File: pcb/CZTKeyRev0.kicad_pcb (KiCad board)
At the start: 2 copper layers, 327.8 x 176.2 mm, 166 parts, among them U1 proton_c

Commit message: Edits to layout and sutff
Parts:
- removed D73: D_Small, Diode_THT:D_DO-35_SOD27_P5.08mm_Vertical_KathodeUp
- moved D45 487.8 mm to (57.8, 36.5), turned to 270 degrees
- moved D30 485.9 mm to (54.6, 36.5), turned to 270 degrees
- moved D15 436.1 mm to (51.4, 36.5), turned to 270 degrees
- moved D1 27.2 mm to (48.3, 36.5)
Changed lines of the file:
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@@
     (tracks 0)
     (zones 0)
-    (modules 166)
+    (modules 165)
     (nets 154)
   )
@@
   )
   (module Diode_THT:D_DO-35_SOD27_P5.08mm_Vertical_KathodeUp (layer F.Cu)
-    (at 182.41375 -185.63375)
-    (descr "Diode, DO-35_SOD27 series, Axial, Vertical, pin pitch=5.08mm, , length*diameter=4*2mm^2, , http://www.diodes.com/_files/packages/DO-35.pdf")
-    (tags "Diode DO-35_SOD27 series Axial Vertical pin pitch 5.08mm  length 4mm diameter 2mm")
-    (fp_text reference D73 (at 2.54 -2.326371) (layer F.SilkS)
-      (effects (font (size 1 1) (thickness 0.15)))
-    )
-    (fp_text value D_Small (at 2.54 2.326371) (layer F.Fab)
-      (effects (font (size 1 1) (thickness 0.15)))
-    )
-    (fp_text user K (at 1.5 0.8) (layer F.SilkS)
-      (effects (font (size 1 1) (thickness 0.15)))
-    )
-    (fp_text user K (at 1.5 0.8) (layer F.Fab)
-      (effects (font (size 1 1) (thickness 0.15)))
-    )
-    (fp_text user %R (at 2.54 -2.326371) (layer F.Fab)
-      (effects (font (size 1 1) (thickness 0.15)))
-    )
-    (fp_line (start 6.33 -1.25) (end -1.05 -1.25) (layer F.CrtYd) (width 0.05))
-    (fp_line (start 6.33 1.25) (end 6.33 -1.25) (layer F.CrtYd) (width 0.05))
-    (fp_line (start -1.05 1.25) (end 6.33 1.25) (layer F.CrtYd) (width 0.05))
-    (fp_line (start -1.05 -1.25) (end -1.05 1.25) (layer F.CrtYd) (width 0.05))
-    (fp_line (start 3.753629 0) (end 1.1 0) (layer F.SilkS) (width 0.12))
-    (fp_line (start 0 0) (end 5.08 0) (layer F.Fab) (width 0.1))
-    (fp_circle (center 5.08 0) (end 6.406371 0) (layer F.SilkS) (width 0.12))
-    (fp_circle (center 5.08 0) (end 6.08 0) (layer F.Fab) (width 0.1))
-    (pad 2 thru_hole oval (at 5.08 0) (size 1.6 1.6) (drill 0.8) (layers *.Cu *.Mask)
-      (net 78 "Net-(D73-Pad2)"))
-    (pad 1 thru_hole rect (at 0 0) (size 1.6 1.6) (drill 0.8) (layers *.Cu *.Mask)
-      (net 79 ROW5))
-    (model ${KISYS3DMOD}/Diode_THT.3dshapes/D_DO-35_SOD27_P5.08mm_Vertical_KathodeUp.wrl
-      (at (xyz 0 0 0))
-      (scale (xyz 1 1 1))
-      (rotate (xyz 0 0 0))
-    )
-  )
-  (module Diode_THT:D_DO-35_SOD27_P5.08mm_Vertical_KathodeUp (layer F.Cu)
     (at 189.10375 -99.81375)
     (descr "Diode, DO-35_SOD27 series, Axial, Vertical, pin pitch=5.08mm, , length*diameter=4*2mm^2, , http://www.diodes.com/_files/packages/DO-35.pdf")
@@
   )
   (module Diode_THT:D_DO-35_SOD27_P5.08mm_Vertical_KathodeUp (layer F.Cu)
-    (at 448.90375 -255.05375)
+    (at 57.785 36.5125 270)
     (descr "Diode, DO-35_SOD27 series, Axial, Vertical, pin pitch=5.08mm, , length*diameter=4*2mm^2, , http://www.diodes.com/_files/packages/DO-35.pdf")
     (tags "Diode DO-35_SOD27 series Axial Vertical pin pitch 5.08mm  length 4mm diameter 2mm")
-    (fp_text reference D45 (at 2.54 -2.326371) (layer F.SilkS)
+    (fp_text reference D45 (at 2.54 -2.326371 90) (layer F.SilkS)
       (effects (font (size 1 1) (thickness 0.15)))
     )
-    (fp_text value D_Small (at 2.54 2.326371) (layer F.Fab)
+    (fp_text value D_Small (at 2.54 2.326371 90) (layer F.Fab)
       (effects (font (size 1 1) (thickness 0.15)))
     )
-    (fp_text user K (at 1.5 0.8) (layer F.SilkS)
+    (fp_text user K (at 1.5 0.8 90) (layer F.SilkS)
       (effects (font (size 1 1) (thickness 0.15)))
     )
-    (fp_text user K (at 1.5 0.8) (layer F.Fab)
+    (fp_text user K (at 1.5 0.8 90) (layer F.Fab)
       (effects (font (size 1 1) (thickness 0.15)))
     )
-    (fp_text user %R (at 2.54 -2.326371) (layer F.Fab)
+    (fp_text user %R (at 2.54 -2.326371 90) (layer F.Fab)
       (effects (font (size 1 1) (thickness 0.15)))
     )
@@
     (fp_circle (center 5.08 0) (end 6.406371 0) (layer F.SilkS) (width 0.12))
     (fp_circle (center 5.08 0) (end 6.08 0) (layer F.Fab) (width 0.1))
-    (pad 2 thru_hole oval (at 5.08 0) (size 1.6 1.6) (drill 0.8) (layers *.Cu *.Mask)
+    (pad 2 thru_hole oval (at 5.08 0 270) (size 1.6 1.6) (drill 0.8) (layers *.Cu *.Mask)
       (net 48 "Net-(D45-Pad2)"))
-    (pad 1 thru_hole rect (at 0 0) (size 1.6 1.6) (drill 0.8) (layers *.Cu *.Mask)
+    (pad 1 thru_hole rect (at 0 0 270) (size 1.6 1.6) (drill 0.8) (layers *.Cu *.Mask)
       (net 49 ROW3))
     (model ${KISYS3DMOD}/Diode_THT.3dshapes/D_DO-35_SOD27_P5.08mm_Vertical_KathodeUp.wrl
@@
   )
   (module Diode_THT:D_DO-35_SOD27_P5.08mm_Vertical_KathodeUp (layer F.Cu)
-    (at 448.90375 -247.51375)
+    (at 54.61 36.5125 270)
     (descr "Diode, DO-35_SOD27 series, Axial, Vertical, pin pitch=5.08mm, , length*diameter=4*2mm^2, , http://www.diodes.com/_files/packages/DO-35.pdf")
     (tags "Diode DO-35_SOD27 series Axial Vertical pin pitch 5.08mm  length 4mm diameter 2mm")
-    (fp_text reference D30 (at 2.54 -2.326371) (layer F.SilkS)
+    (fp_text reference D30 (at 2.54 -2.326371 90) (layer F.SilkS)
       (effects (font (size 1 1) (thickness 0.15)))
     )
-    (fp_text value D_Small (at 2.54 2.326371) (layer F.Fab)
+    (fp_text value D_Small (at 2.54 2.326371 90) (layer F.Fab)
       (effects (font (size 1 1) (thickness 0.15)))
     )
-    (fp_text user K (at 1.5 0.8) (layer F.SilkS)
+    (fp_text user K (at 1.5 0.8 90) (layer F.SilkS)
       (effects (font (size 1 1) (thickness 0.15)))
     )
-    (fp_text user K (at 1.5 0.8) (layer F.Fab)
+    (fp_text user K (at 1.5 0.8 90) (layer F.Fab)
       (effects (font (size 1 1) (thickness 0.15)))
     )
-    (fp_text user %R (at 2.54 -2.326371) (layer F.Fab)
+    (fp_text user %R (at 2.54 -2.326371 90) (layer F.Fab)
       (effects (font (size 1 1) (thickness 0.15)))
     )
@@
     (fp_circle (center 5.08 0) (end 6.406371 0) (layer F.SilkS) (width 0.12))
     (fp_circle (center 5.08 0) (end 6.08 0) (layer F.Fab) (width 0.1))
-    (pad 2 thru_hole oval (at 5.08 0) (size 1.6 1.6) (drill 0.8) (layers *.Cu *.Mask)
+    (pad 2 thru_hole oval (at 5.08 0 270) (size 1.6 1.6) (drill 0.8) (layers *.Cu *.Mask)
       (net 32 "Net-(D30-Pad2)"))
-    (pad 1 thru_hole rect (at 0 0) (size 1.6 1.6) (drill 0.8) (layers *.Cu *.Mask)
+    (pad 1 thru_hole rect (at 0 0 270) (size 1.6 1.6) (drill 0.8) (layers *.Cu *.Mask)
       (net 33 ROW2))
     (model ${KISYS3DMOD}/Diode_THT.3dshapes/D_DO-35_SOD27_P5.08mm_Vertical_KathodeUp.wrl
@@
   )
   (module Diode_THT:D_DO-35_SOD27_P5.08mm_Vertical_KathodeUp (layer F.Cu)
-    (at 423.65375 -190.68375)
+    (at 51.435 36.5125 270)
     (descr "Diode, DO-35_SOD27 series, Axial, Vertical, pin pitch=5.08mm, , length*diameter=4*2mm^2, , http://www.diodes.com/_files/packages/DO-35.pdf")
     (tags "Diode DO-35_SOD27 series Axial Vertical pin pitch 5.08mm  length 4mm diameter 2mm")
-    (fp_text reference D15 (at 2.54 -2.326371) (layer F.SilkS)
+    (fp_text reference D15 (at 2.54 -2.326371 90) (layer F.SilkS)
       (effects (font (size 1 1) (thickness 0.15)))
     )
-    (fp_text value D_Small (at 2.54 2.326371) (layer F.Fab)
+    (fp_text value D_Small (at 2.54 2.326371 90) (layer F.Fab)
       (effects (font (size 1 1) (thickness 0.15)))
     )
-    (fp_text user K (at 1.5 0.8) (layer F.SilkS)
+    (fp_text user K (at 1.5 0.8 90) (layer F.SilkS)
       (effects (font (size 1 1) (thickness 0.15)))
     )
-    (fp_text user K (at 1.5 0.8) (layer F.Fab)
+    (fp_text user K (at 1.5 0.8 90) (layer F.Fab)
       (effects (font (size 1 1) (thickness 0.15)))
     )
-    (fp_text user %R (at 2.54 -2.326371) (layer F.Fab)
+    (fp_text user %R (at 2.54 -2.326371 90) (layer F.Fab)
       (effects (font (size 1 1) (thickness 0.15)))
     )
@@
     (fp_circle (center 5.08 0) (end 6.406371 0) (layer F.SilkS) (width 0.12))
     (fp_circle (center 5.08 0) (end 6.08 0) (layer F.Fab) (width 0.1))
-    (pad 2 thru_hole oval (at 5.08 0) (size 1.6 1.6) (drill 0.8) (layers *.Cu *.Mask)
+    (pad 2 thru_hole oval (at 5.08 0 270) (size 1.6 1.6) (drill 0.8) (layers *.Cu *.Mask)
       (net 16 "Net-(D15-Pad2)"))
-    (pad 1 thru_hole rect (at 0 0) (size 1.6 1.6) (drill 0.8) (layers *.Cu *.Mask)
+    (pad 1 thru_hole rect (at 0 0 270) (size 1.6 1.6) (drill 0.8) (layers *.Cu *.Mask)
       (net 17 ROW1))
     (model ${KISYS3DMOD}/Diode_THT.3dshapes/D_DO-35_SOD27_P5.08mm_Vertical_KathodeUp.wrl
@@
   )
   (module Diode_THT:D_DO-35_SOD27_P5.08mm_Vertical_KathodeUp (layer F.Cu)
-    (at 75.40625 34.925 270)
+    (at 48.26 36.5125 270)
     (descr "Diode, DO-35_SOD27 series, Axial, Vertical, pin pitch=5.08mm, , length*diameter=4*2mm^2, , http://www.diodes.com/_files/packages/DO-35.pdf")
     (tags "Diode DO-35_SOD27 series Axial Vertical pin pitch 5.08mm  length 4mm diameter 2mm")

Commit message: Positioned things
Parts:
- added C1: 100n, Capacitor_SMD:C_0603_1608Metric, F.Cu at (12.7, 77.0)
- added C2: 100n, Capacitor_SMD:C_0603_1608Metric, F.Cu at (-10.3, 77.0)
- added D73: D_Small, Diode_THT:D_DO-35_SOD27_P5.08mm_Vertical_KathodeUp, F.Cu at (197.6, 46.0)
- added D82: D_Small, Diode_THT:D_DO-35_SOD27_P5.08mm_Vertical_KathodeUp, F.Cu at (53.2, 46.0)
- added D83: D_Small, Diode_THT:D_DO-35_SOD27_P5.08mm_Vertical_KathodeUp, F.Cu at (56.4, 46.0)
- added D84: D_Small, Diode_THT:D_DO-35_SOD27_P5.08mm_Vertical_KathodeUp, F.Cu at (59.5, 46.0)
- added D85: D_Small, Diode_THT:D_DO-35_SOD27_P5.08mm_Vertical_KathodeUp, F.Cu at (62.7, 46.0)
- added D86: D_Small, Diode_THT:D_DO-35_SOD27_P5.08mm_Vertical_KathodeUp, F.Cu at (65.9, 46.0)
- added MX_MAC1: MX-NoLED, MX_Alps_Hybrid:MX-1U-NoLED, F.Cu at (1.59, 104.8)
- added MX_MAC2: MX-NoLED, MX_Alps_Hybrid:MX-1U-NoLED, F.Cu at (1.59, 123.8)
- added MX_MAC3: MX-NoLED, MX_Alps_Hybrid:MX-1U-NoLED, F.Cu at (1.59, 142.9)
- added MX_MAC4: MX-NoLED, MX_Alps_Hybrid:MX-1U-NoLED, F.Cu at (1.59, 161.9)
- added MX_MAC5: MX-NoLED, MX_Alps_Hybrid:MX-1U-NoLED, F.Cu at (1.59, 181.0)
- added R1: 10k, Resistor_SMD:R_Array_Convex_4x0603, F.Cu at (-9.53, 87.3)
- added R2: 10k, Resistor_SMD:R_Array_Convex_4x0603, F.Cu at (11.9, 87.3)
- added R3: 10K, Resistor_SMD:R_Array_Convex_4x0603, F.Cu at (-9.53, 82.5)
- added R4: 10K, Resistor_SMD:R_Array_Convex_4x0603, F.Cu at (11.9, 82.5)
- added R5: 10K, Resistor_SMD:R_0603_1608Metric, F.Cu at (303.7, 62.0)
- added WS1: WS2812B, WS2812B-edited:Neopixel_easy_LED_WS2812B_PLCC4_5.0x5.0mm_P3.2mm, F.Cu at (25.2, 74.0)
- added WS10: WS2812B, WS2812B-edited:Neopixel_easy_LED_WS2812B_PLCC4_5.0x5.0mm_P3.2mm, F.Cu at (211.2, 74.0)
- added WS11: WS2812B, WS2812B-edited:Neopixel_easy_LED_WS2812B_PLCC4_5.0x5.0mm_P3.2mm, F.Cu at (230.2, 74.0)
- added WS12: WS2812B, WS2812B-edited:Neopixel_easy_LED_WS2812B_PLCC4_5.0x5.0mm_P3.2mm, F.Cu at (249.2, 74.0)
- added WS13: WS2812B, WS2812B-edited:Neopixel_easy_LED_WS2812B_PLCC4_5.0x5.0mm_P3.2mm, F.Cu at (268.5, 74.0)
- added WS14: WS2812B, WS2812B-edited:Neopixel_easy_LED_WS2812B_PLCC4_5.0x5.0mm_P3.2mm, F.Cu at (292.2, 74.0)
- added WS15: WS2812B, WS2812B-edited:Neopixel_easy_LED_WS2812B_PLCC4_5.0x5.0mm_P3.2mm, F.Cu at (1.50, 97.8)
- added WS16: WS2812B, WS2812B-edited:Neopixel_easy_LED_WS2812B_PLCC4_5.0x5.0mm_P3.2mm, F.Cu at (26.0, 97.8)
- added WS17: WS2812B, WS2812B-edited:Neopixel_easy_LED_WS2812B_PLCC4_5.0x5.0mm_P3.2mm, F.Cu at (44.5, 97.8)
- added WS18: WS2812B, WS2812B-edited:Neopixel_easy_LED_WS2812B_PLCC4_5.0x5.0mm_P3.2mm, F.Cu at (63.5, 97.8)
- added WS19: WS2812B, WS2812B-edited:Neopixel_easy_LED_WS2812B_PLCC4_5.0x5.0mm_P3.2mm, F.Cu at (82.5, 97.8)
- added WS2: WS2812B, WS2812B-edited:Neopixel_easy_LED_WS2812B_PLCC4_5.0x5.0mm_P3.2mm, F.Cu at (49.2, 74.0)
- added WS20: WS2812B, WS2812B-edited:Neopixel_easy_LED_WS2812B_PLCC4_5.0x5.0mm_P3.2mm, F.Cu at (101.5, 97.8)
- added WS21: WS2812B, WS2812B-edited:Neopixel_easy_LED_WS2812B_PLCC4_5.0x5.0mm_P3.2mm, F.Cu at (120.5, 97.8)
- added WS22: WS2812B, WS2812B-edited:Neopixel_easy_LED_WS2812B_PLCC4_5.0x5.0mm_P3.2mm, F.Cu at (139.8, 97.8)
- added WS23: WS2812B, WS2812B-edited:Neopixel_easy_LED_WS2812B_PLCC4_5.0x5.0mm_P3.2mm, F.Cu at (158.8, 97.8)
- added WS24: WS2812B, WS2812B-edited:Neopixel_easy_LED_WS2812B_PLCC4_5.0x5.0mm_P3.2mm, F.Cu at (177.8, 97.8)
- added WS25: WS2812B, WS2812B-edited:Neopixel_easy_LED_WS2812B_PLCC4_5.0x5.0mm_P3.2mm, F.Cu at (196.8, 97.8)
- added WS26: WS2812B, WS2812B-edited:Neopixel_easy_LED_WS2812B_PLCC4_5.0x5.0mm_P3.2mm, F.Cu at (216.0, 97.8)
- added WS27: WS2812B, WS2812B-edited:Neopixel_easy_LED_WS2812B_PLCC4_5.0x5.0mm_P3.2mm, F.Cu at (235.0, 97.8)
- added WS28: WS2812B, WS2812B-edited:Neopixel_easy_LED_WS2812B_PLCC4_5.0x5.0mm_P3.2mm, F.Cu at (254.0, 97.8)
- added WS29: WS2812B, WS2812B-edited:Neopixel_easy_LED_WS2812B_PLCC4_5.0x5.0mm_P3.2mm, F.Cu at (282.5, 97.8)
- added WS3: WS2812B, WS2812B-edited:Neopixel_easy_LED_WS2812B_PLCC4_5.0x5.0mm_P3.2mm, F.Cu at (68.2, 74.0)
- added WS30: WS2812B, WS2812B-edited:Neopixel_easy_LED_WS2812B_PLCC4_5.0x5.0mm_P3.2mm, F.Cu at (325.2, 97.8)
- added WS31: WS2812B, WS2812B-edited:Neopixel_easy_LED_WS2812B_PLCC4_5.0x5.0mm_P3.2mm, F.Cu at (1.50, 116.8)
- added WS32: WS2812B, WS2812B-edited:Neopixel_easy_LED_WS2812B_PLCC4_5.0x5.0mm_P3.2mm, F.Cu at (30.0, 116.8)
- added WS33: WS2812B, WS2812B-edited:Neopixel_easy_LED_WS2812B_PLCC4_5.0x5.0mm_P3.2mm, F.Cu at (54.0, 116.8)
- added WS34: WS2812B, WS2812B-edited:Neopixel_easy_LED_WS2812B_PLCC4_5.0x5.0mm_P3.2mm, F.Cu at (73.0, 116.8)
- added WS35: WS2812B, WS2812B-edited:Neopixel_easy_LED_WS2812B_PLCC4_5.0x5.0mm_P3.2mm, F.Cu at (92.0, 116.8)
- added WS36: WS2812B, WS2812B-edited:Neopixel_easy_LED_WS2812B_PLCC4_5.0x5.0mm_P3.2mm, F.Cu at (111.0, 116.8)
- added WS37: WS2812B, WS2812B-edited:Neopixel_easy_LED_WS2812B_PLCC4_5.0x5.0mm_P3.2mm, F.Cu at (130.2, 116.8)
- added WS38: WS2812B, WS2812B-edited:Neopixel_easy_LED_WS2812B_PLCC4_5.0x5.0mm_P3.2mm, F.Cu at (149.2, 116.8)
- added WS39: WS2812B, WS2812B-edited:Neopixel_easy_LED_WS2812B_PLCC4_5.0x5.0mm_P3.2mm, F.Cu at (168.2, 116.8)
- added WS4: WS2812B, WS2812B-edited:Neopixel_easy_LED_WS2812B_PLCC4_5.0x5.0mm_P3.2mm, F.Cu at (87.5, 74.0)
- added WS40: WS2812B, WS2812B-edited:Neopixel_easy_LED_WS2812B_PLCC4_5.0x5.0mm_P3.2mm, F.Cu at (187.2, 116.8)
- added WS41: WS2812B, WS2812B-edited:Neopixel_easy_LED_WS2812B_PLCC4_5.0x5.0mm_P3.2mm, F.Cu at (206.2, 116.8)
- added WS42: WS2812B, WS2812B-edited:Neopixel_easy_LED_WS2812B_PLCC4_5.0x5.0mm_P3.2mm, F.Cu at (225.5, 116.8)
- added WS43: WS2812B, WS2812B-edited:Neopixel_easy_LED_WS2812B_PLCC4_5.0x5.0mm_P3.2mm, F.Cu at (244.5, 116.8)
- added WS44: WS2812B, WS2812B-edited:Neopixel_easy_LED_WS2812B_PLCC4_5.0x5.0mm_P3.2mm, F.Cu at (263.5, 116.8)
- added WS45: WS2812B, WS2812B-edited:Neopixel_easy_LED_WS2812B_PLCC4_5.0x5.0mm_P3.2mm, F.Cu at (287.2, 116.8)
- added WS46: WS2812B, WS2812B-edited:Neopixel_easy_LED_WS2812B_PLCC4_5.0x5.0mm_P3.2mm, F.Cu at (325.5, 116.8)
- added WS47: WS2812B, WS2812B-edited:Neopixel_easy_LED_WS2812B_PLCC4_5.0x5.0mm_P3.2mm, F.Cu at (1.50, 135.8)
- added WS48: WS2812B, WS2812B-edited:Neopixel_easy_LED_WS2812B_PLCC4_5.0x5.0mm_P3.2mm, F.Cu at (32.2, 135.8)
- added WS49: WS2812B, WS2812B-edited:Neopixel_easy_LED_WS2812B_PLCC4_5.0x5.0mm_P3.2mm, F.Cu at (58.8, 135.8)
- added WS5: WS2812B, WS2812B-edited:Neopixel_easy_LED_WS2812B_PLCC4_5.0x5.0mm_P3.2mm, F.Cu at (106.2, 74.0)
- added WS50: WS2812B, WS2812B-edited:Neopixel_easy_LED_WS2812B_PLCC4_5.0x5.0mm_P3.2mm, F.Cu at (77.8, 135.8)
- added WS51: WS2812B, WS2812B-edited:Neopixel_easy_LED_WS2812B_PLCC4_5.0x5.0mm_P3.2mm, F.Cu at (96.8, 135.8)
- added WS52: WS2812B, WS2812B-edited:Neopixel_easy_LED_WS2812B_PLCC4_5.0x5.0mm_P3.2mm, F.Cu at (115.8, 135.8)
- added WS53: WS2812B, WS2812B-edited:Neopixel_easy_LED_WS2812B_PLCC4_5.0x5.0mm_P3.2mm, F.Cu at (135.0, 135.8)
- added WS54: WS2812B, WS2812B-edited:Neopixel_easy_LED_WS2812B_PLCC4_5.0x5.0mm_P3.2mm, F.Cu at (154.0, 135.8)
- added WS55: WS2812B, WS2812B-edited:Neopixel_easy_LED_WS2812B_PLCC4_5.0x5.0mm_P3.2mm, F.Cu at (173.0, 135.8)
- added WS56: WS2812B, WS2812B-edited:Neopixel_easy_LED_WS2812B_PLCC4_5.0x5.0mm_P3.2mm, F.Cu at (192.0, 135.8)
- added WS57: WS2812B, WS2812B-edited:Neopixel_easy_LED_WS2812B_PLCC4_5.0x5.0mm_P3.2mm, F.Cu at (211.0, 135.8)
- added WS58: WS2812B, WS2812B-edited:Neopixel_easy_LED_WS2812B_PLCC4_5.0x5.0mm_P3.2mm, F.Cu at (230.0, 135.8)
- added WS59: WS2812B, WS2812B-edited:Neopixel_easy_LED_WS2812B_PLCC4_5.0x5.0mm_P3.2mm, F.Cu at (249.2, 135.8)
- added WS6: WS2812B, WS2812B-edited:Neopixel_easy_LED_WS2812B_PLCC4_5.0x5.0mm_P3.2mm, F.Cu at (130.2, 74.0)
- added WS60: WS2812B, WS2812B-edited:Neopixel_easy_LED_WS2812B_PLCC4_5.0x5.0mm_P3.2mm, F.Cu at (280.0, 135.8)
- added WS61: WS2812B, WS2812B-edited:Neopixel_easy_LED_WS2812B_PLCC4_5.0x5.0mm_P3.2mm, F.Cu at (325.5, 135.8)
- added WS62: WS2812B, WS2812B-edited:Neopixel_easy_LED_WS2812B_PLCC4_5.0x5.0mm_P3.2mm, F.Cu at (1.50, 155.0)
- added WS63: WS2812B, WS2812B-edited:Neopixel_easy_LED_WS2812B_PLCC4_5.0x5.0mm_P3.2mm, F.Cu at (37.5, 155.0)
- added WS64: WS2812B, WS2812B-edited:Neopixel_easy_LED_WS2812B_PLCC4_5.0x5.0mm_P3.2mm, F.Cu at (68.2, 155.0)
- added WS65: WS2812B, WS2812B-edited:Neopixel_easy_LED_WS2812B_PLCC4_5.0x5.0mm_P3.2mm, F.Cu at (87.2, 155.0)
- added WS66: WS2812B, WS2812B-edited:Neopixel_easy_LED_WS2812B_PLCC4_5.0x5.0mm_P3.2mm, F.Cu at (106.2, 155.0)
- added WS67: WS2812B, WS2812B-edited:Neopixel_easy_LED_WS2812B_PLCC4_5.0x5.0mm_P3.2mm, F.Cu at (125.2, 155.0)
- added WS68: WS2812B, WS2812B-edited:Neopixel_easy_LED_WS2812B_PLCC4_5.0x5.0mm_P3.2mm, F.Cu at (144.5, 155.0)
- added WS69: WS2812B, WS2812B-edited:Neopixel_easy_LED_WS2812B_PLCC4_5.0x5.0mm_P3.2mm, F.Cu at (163.5, 155.0)
- added WS7: WS2812B, WS2812B-edited:Neopixel_easy_LED_WS2812B_PLCC4_5.0x5.0mm_P3.2mm, F.Cu at (149.2, 74.0)
- added WS70: WS2812B, WS2812B-edited:Neopixel_easy_LED_WS2812B_PLCC4_5.0x5.0mm_P3.2mm, F.Cu at (182.5, 155.0)
- added WS71: WS2812B, WS2812B-edited:Neopixel_easy_LED_WS2812B_PLCC4_5.0x5.0mm_P3.2mm, F.Cu at (201.5, 155.0)
- added WS72: WS2812B, WS2812B-edited:Neopixel_easy_LED_WS2812B_PLCC4_5.0x5.0mm_P3.2mm, F.Cu at (220.5, 155.0)
- added WS73: WS2812B, WS2812B-edited:Neopixel_easy_LED_WS2812B_PLCC4_5.0x5.0mm_P3.2mm, F.Cu at (239.8, 155.0)
- added WS74: WS2812B, WS2812B-edited:Neopixel_easy_LED_WS2812B_PLCC4_5.0x5.0mm_P3.2mm, F.Cu at (266.0, 155.0)
- added WS75: WS2812B, WS2812B-edited:Neopixel_easy_LED_WS2812B_PLCC4_5.0x5.0mm_P3.2mm, F.Cu at (301.8, 159.8)
- added WS76: WS2812B, WS2812B-edited:Neopixel_easy_LED_WS2812B_PLCC4_5.0x5.0mm_P3.2mm, F.Cu at (325.5, 155.0)
- added WS77: WS2812B, WS2812B-edited:Neopixel_easy_LED_WS2812B_PLCC4_5.0x5.0mm_P3.2mm, F.Cu at (1.50, 174.2)
- added WS78: WS2812B, WS2812B-edited:Neopixel_easy_LED_WS2812B_PLCC4_5.0x5.0mm_P3.2mm, F.Cu at (27.8, 174.0)
- added WS79: WS2812B, WS2812B-edited:Neopixel_easy_LED_WS2812B_PLCC4_5.0x5.0mm_P3.2mm, F.Cu at (51.5, 174.0)
- added WS8: WS2812B, WS2812B-edited:Neopixel_easy_LED_WS2812B_PLCC4_5.0x5.0mm_P3.2mm, F.Cu at (168.2, 74.0)
- added WS80: WS2812B, WS2812B-edited:Neopixel_easy_LED_WS2812B_PLCC4_5.0x5.0mm_P3.2mm, F.Cu at (75.5, 174.0)
- added WS81: WS2812B, WS2812B-edited:Neopixel_easy_LED_WS2812B_PLCC4_5.0x5.0mm_P3.2mm, F.Cu at (147.0, 174.0)
- added WS82: WS2812B, WS2812B-edited:Neopixel_easy_LED_WS2812B_PLCC4_5.0x5.0mm_P3.2mm, F.Cu at (220.5, 174.0)
- added WS83: WS2812B, WS2812B-edited:Neopixel_easy_LED_WS2812B_PLCC4_5.0x5.0mm_P3.2mm, F.Cu at (249.2, 174.0)
- added WS84: WS2812B, WS2812B-edited:Neopixel_easy_LED_WS2812B_PLCC4_5.0x5.0mm_P3.2mm, F.Cu at (282.5, 178.8)
- added WS85: WS2812B, WS2812B-edited:Neopixel_easy_LED_WS2812B_PLCC4_5.0x5.0mm_P3.2mm, F.Cu at (301.8, 178.8)
- added WS86: WS2812B, WS2812B-edited:Neopixel_easy_LED_WS2812B_PLCC4_5.0x5.0mm_P3.2mm, F.Cu at (320.8, 178.8)
- added WS9: WS2812B, WS2812B-edited:Neopixel_easy_LED_WS2812B_PLCC4_5.0x5.0mm_P3.2mm, F.Cu at (187.5, 74.0)
- moved D31 456.8 mm to (77.0, 36.5), turned to 270 degrees
- moved D39 439.6 mm to (115.1, 46.0), turned to 270 degrees
- moved D17 435.3 mm to (73.8, 46.0), turned to 270 degrees
- moved D34 431.7 mm to (97.6, 46.0), turned to 270 degrees
- moved D18 424.2 mm to (94.5, 36.5), turned to 270 degrees
- moved D33 416.9 mm to (97.6, 36.5), turned to 270 degrees
- moved D36 412.8 mm to (135.7, 36.5), turned to 270 degrees
- moved D6 410.4 mm to (108.7, 36.5), turned to 270 degrees
- moved D40 407.4 mm to (153.2, 36.5), turned to 270 degrees
- moved D44 407.2 mm to (170.7, 46.0), turned to 270 degrees
- moved D24 406.7 mm to (111.9, 46.0), turned to 270 degrees
- moved D35 405.3 mm to (115.1, 36.5), turned to 270 degrees
- moved D41 401.1 mm to (153.2, 46.0), turned to 270 degrees
- moved D29 388.0 mm to (167.5, 46.0), turned to 270 degrees
- moved D21 387.0 mm to (132.6, 36.5), turned to 270 degrees
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- renumbered MX_F13 to MX_F0
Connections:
- ENC1 pad C: Net-(ENC1-PadC) -> +5V
- ENC1 pad S1: Net-(ENC1-PadS1) -> VCC
- ENC1 pad S2: Net-(ENC1-PadS2) -> ENC_SW
- MX_0 pad 1: COL10 -> COL11
- MX_1 pad 1: COL1 -> COL2
- MX_2 pad 1: COL2 -> COL3
- MX_3 pad 1: COL3 -> COL4
- MX_4 pad 1: COL4 -> COL5
- MX_5 pad 1: COL5 -> COL6
- MX_6 pad 1: COL6 -> COL7
- MX_7 pad 1: COL7 -> COL8
- MX_8 pad 1: COL8 -> COL9
- MX_9 pad 1: COL9 -> COL10
- MX_CAPS1 pad 1: COL0 -> COL1
- MX_CTRL_L1 pad 1: COL0 -> COL1
- MX_CTRL_R1 pad 1: COL12 -> COL11
- MX_DELETE1 pad 1: COL16 -> COL15
- MX_DOWN1 pad 1: COL14 -> COL13
- MX_EQUAL1 pad 1: COL12 -> COL13
- MX_ESC1 pad 1: COL0 -> COL1
- MX_F1 pad 1: COL1 -> COL2
- MX_F2 pad 1: COL2 -> COL3
- MX_F3 pad 1: COL3 -> COL4
- MX_F4 pad 1: COL4 -> COL5
- MX_INSERT1 pad 1: COL16 -> COL15
- MX_LEFT1 pad 1: COL13 -> COL12
- MX_MINUS1 pad 1: COL11 -> COL12
- MX_PGDWN1 pad 1: COL16 -> COL15
- MX_PGUP1 pad 1: COL16 -> COL15
- MX_SHIFT_R1 pad 1: COL13 -> COL12
- MX_TAB1 pad 1: COL0 -> COL1
- MX_TILDE1 pad 1: COL0 -> COL1
- MX_WIN1 pad 1: COL1 -> COL2
- OLED1 pad 1: Net-(OLED1-Pad1) -> GND
- OLED1 pad 2: Net-(OLED1-Pad2) -> VCC
- OLED1 pad 3: Net-(OLED1-Pad3) -> OLEDSCL
- OLED1 pad 4: Net-(OLED1-Pad4) -> OLEDSDA
- U1 pad B10: Net-(U1-PadB10) -> ENC_SW
- U1 pad B11: Net-(U1-PadB11) -> ENC_A
- U1 pad B12: Net-(U1-PadB12) -> ENC_B
- U1 pad B6: Net-(U1-PadB6) -> OLEDSCL
- U1 pad B7: Net-(U1-PadB7) -> OLEDSDA
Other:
- board size 327.8 x 176.2 mm -> 353.8 x 175 mm

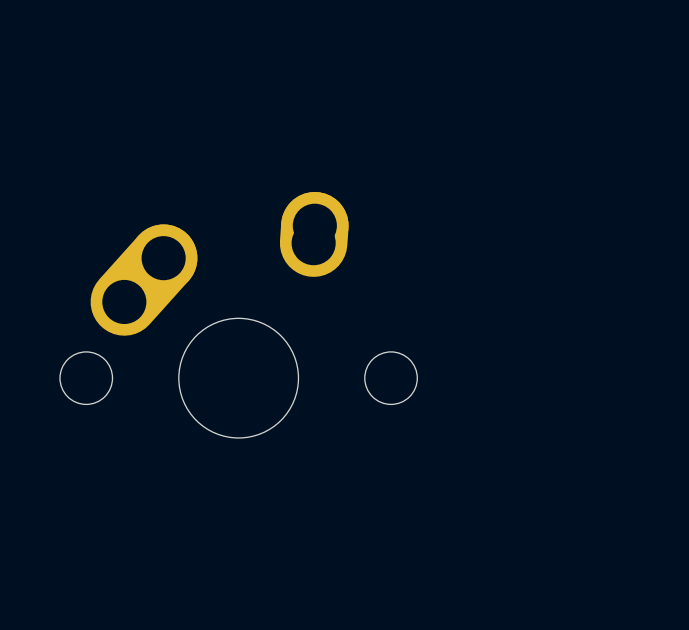
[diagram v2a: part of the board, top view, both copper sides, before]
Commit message: Removed 1.25U spacer
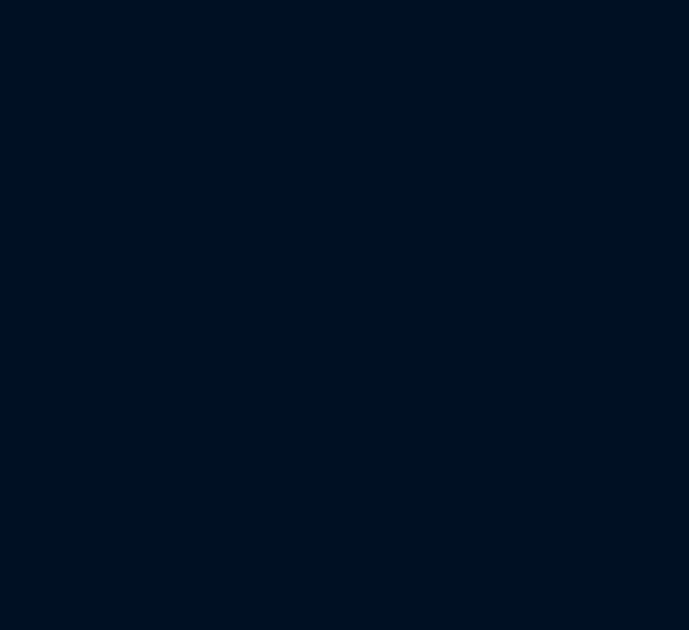
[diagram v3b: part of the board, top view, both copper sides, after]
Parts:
- removed MX_SPACER_125: MX-NoLED, MX_Alps_Hybrid:MX-1.25U-NoLED

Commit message: Maybe final?
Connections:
- U1 pad A0: Net-(U1-PadA0) -> COL2
- U1 pad A1: Net-(U1-PadA1) -> COL1
- U1 pad A13: Net-(U1-PadA13) -> COL15
- U1 pad A14: Net-(U1-PadA14) -> COL14
- U1 pad A15: Net-(U1-PadA15) -> COL13
- U1 pad A2: Net-(U1-PadA2) -> COL0
- U1 pad A4: Net-(U1-PadA4) -> COL8
- U1 pad A5: Net-(U1-PadA5) -> COL9
- U1 pad A6: Net-(U1-PadA6) -> COL10
- U1 pad A7: Net-(U1-PadA7) -> COL11
- U1 pad A8: Net-(U1-PadA8) -> COL12
- U1 pad B0: Net-(U1-PadB0) -> ROW0
- U1 pad B1: Net-(U1-PadB1) -> ROW1
- U1 pad B13: Net-(U1-PadB13) -> COL4
- U1 pad B14: Net-(U1-PadB14) -> COL5
- U1 pad B15: Net-(U1-PadB15) -> COL6
- U1 pad B2: Net-(U1-PadB2) -> ROW2
- U1 pad B3: Net-(U1-PadB3) -> ROW3
- U1 pad B4: Net-(U1-PadB4) -> ROW4
- U1 pad B5: Net-(U1-PadB5) -> ROW5
- U1 pad B8: Net-(U1-PadB8) -> COL3
- U1 pad B9: Net-(U1-PadB9) -> COL7
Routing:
- net GND: track 0.00 -> 2147.2 mm, vias 0 -> 4
- net +5V: track 0.00 -> 2095.9 mm, vias 0 -> 1
- net COL1: track 0.00 -> 447.0 mm, vias 0 -> 2
- net COL0: track 0.00 -> 438.3 mm, vias 0 -> 2
- net COL2: track 0.00 -> 436.8 mm, vias 0 -> 2
- net VCC: track 0.00 -> 409.5 mm, vias 0 -> 1
- net COL3: track 0.00 -> 403.5 mm, vias 0 -> 2
- net COL4: track 0.00 -> 376.9 mm, vias 0 -> 1
- net ENC_SW: track 0.00 -> 357.4 mm
- net ENC_A: track 0.00 -> 357.1 mm, vias 0 -> 1
- net Net-(WS76-Pad2): track 0.00 -> 356.1 mm
- net ROW2: track 0.00 -> 355.8 mm
- net ROW1: track 0.00 -> 352.0 mm
- net ROW0: track 0.00 -> 349.5 mm
- net ROW3: track 0.00 -> 347.3 mm
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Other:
- board outline removed
- net class Default: trace_width 0.25 -> 0.254
- net class Power/GND added: clearance 0.2, trace_width 0.381, via_dia 0.8, via_drill 0.4

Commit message: did some stuff
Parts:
- added REF**: MountingHole_2.2mm_M2_Pad, MountingHole:MountingHole_2.2mm_M2_Pad, F.Cu at (158.8, 182.6)
- added REF**: MountingHole_2.2mm_M2_Pad, MountingHole:MountingHole_2.2mm_M2_Pad, F.Cu at (311.1, 182.6)
- added REF**: MountingHole_2.2mm_M2_Pad, MountingHole:MountingHole_2.2mm_M2_Pad, F.Cu at (13.5, 182.6)
- added REF**: MountingHole_2.2mm_M2_Pad, MountingHole:MountingHole_2.2mm_M2_Pad, F.Cu at (158.8, 90.5)
- added REF**: MountingHole_2.2mm_M2_Pad, MountingHole:MountingHole_2.2mm_M2_Pad, F.Cu at (-3.97, 67.5)
- added REF**: MountingHole_2.2mm_M2_Pad, MountingHole:MountingHole_2.2mm_M2_Pad, F.Cu at (139.7, 67.5)
- added REF**: MountingHole_2.2mm_M2_Pad, MountingHole:MountingHole_2.2mm_M2_Pad, F.Cu at (-3.97, 40.5)
- added REF**: MountingHole_2.2mm_M2_Pad, MountingHole:MountingHole_2.2mm_M2_Pad, F.Cu at (139.7, 40.5)
- added REF**: MountingHole_2.2mm_M2_Pad, MountingHole:MountingHole_2.2mm_M2_Pad, F.Cu at (331.0, 40.5)
- added REF**: MountingHole_2.2mm_M2_Pad, MountingHole:MountingHole_2.2mm_M2_Pad, F.Cu at (331.0, 67.5)
- added REF**: MountingHole_2.2mm_M2_Pad, MountingHole:MountingHole_2.2mm_M2_Pad, F.Cu at (312.7, 74.6)
- added WS87: WS2812B, WS2812B-edited:Neopixel_easy_LED_WS2812B_PLCC4_5.0x5.0mm_P3.2mm, F.Cu at (320.8, 178.8)
- moved R5 299.8 mm to (3.97, 67.5), turned to 180 degrees
- moved WS82 44.8 mm to (176.2, 181.0)
- moved WS84 33.6 mm to (249.2, 174.0)
- moved D14 29.4 mm to (212.7, 55.6)
- moved D23 29.4 mm to (215.9, 46.0)
- moved D28 29.4 mm to (215.9, 55.6)
- moved D38 29.4 mm to (219.1, 46.0)
- moved D43 29.4 mm to (219.1, 55.6)
- moved D53 29.4 mm to (222.3, 46.0)
- moved D67 29.4 mm to (225.4, 46.0)
- moved D71 29.4 mm to (222.3, 55.6)
- moved D73 29.4 mm to (225.4, 55.6)
- moved D9 29.4 mm to (212.7, 46.0)
- moved WS81 28.8 mm to (119.1, 181.0)
- moved WS83 28.8 mm to (220.5, 174.0)
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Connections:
- WS83 pad 4: Net-(WS82-Pad2) -> Net-(WS83-Pad4)
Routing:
- net GND: track 2147.2 -> 0.00 mm, vias 4 -> 0
- net +5V: track 2095.9 -> 0.00 mm, vias 1 -> 0
- net COL1: track 447.0 -> 0.00 mm, vias 2 -> 0
- net COL0: track 438.3 -> 0.00 mm, vias 2 -> 0
- net COL2: track 436.8 -> 0.00 mm, vias 2 -> 0
- net VCC: track 409.5 -> 0.00 mm, vias 1 -> 0
- net COL3: track 403.5 -> 0.00 mm, vias 2 -> 0
- net COL4: track 376.9 -> 0.00 mm, vias 1 -> 0
- net ENC_SW: track 357.4 -> 0.00 mm
- net ENC_A: track 357.1 -> 0.00 mm, vias 1 -> 0
- net Net-(WS76-Pad2): track 356.1 -> 0.00 mm
- net ROW2: track 355.8 -> 0.00 mm
- net ROW1: track 352.0 -> 0.00 mm
- net ROW0: track 349.5 -> 0.00 mm
- net ROW3: track 347.3 -> 0.00 mm
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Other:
- board outline added: 343 x 159 mm
